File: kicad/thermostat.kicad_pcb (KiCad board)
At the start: 2 copper layers, 65 x 56 mm, 5 parts, among them P1 Conn_02x20_Odd_Even

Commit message: some board changes, probably too small...
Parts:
- added SW_DOWN1: SW_DOWN, Buttons_Switches_SMD:SW_SPST_EVPBF, F.Cu at (249.5, 141.7)
- added SW_ENTER1: SW_ENTER, Buttons_Switches_SMD:SW_SPST_EVPBF, F.Cu at (227.3, 141.7)
- added SW_MODE1: SW_MODE, Buttons_Switches_SMD:SW_SPST_EVPBF, F.Cu at (238.7, 141.7)
- added SW_UP1: SW_UP, Buttons_Switches_SMD:SW_SPST_EVPBF, F.Cu at (215.9, 141.7)
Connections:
- net +3V3 renamed /PWR_3.3V
- net +5V renamed /PWR_5V
- net GND renamed /GND
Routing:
- net /GPIO16: track 0.00 -> 54.5 mm
- net /GPIO21(SPI1_SCK): track 0.00 -> 52.2 mm
- net /GPIO17(GEN0): track 0.00 -> 49.2 mm
- net /GPIO22(GEN3): track 0.00 -> 46.6 mm
- added copper zone on B.Cu, net /GND
- added copper zone on F.Cu, net /PWR_3.3V
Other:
- outline, holes or cut-outs redrawn
- board text removed: "CAMERA"
- board text removed: "RASPBERRY-PI 40-PIN ADDON BOARD VIEW FROM TOP NOTE: P1 SHOULD BE FITTED ON THE REVERSE OF THE BOARD ADD EDGE CUTS FROM CAMERA AND DISPLAY PORTS AS REQUIRED"
- board text removed: "RJ45"
- board text removed: "USB"

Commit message: updates
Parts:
- added U1: PanasonicRelay, project_footprints:AGQ210A03, F.Cu at (281.3, 103.0)
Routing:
- net /GND: track 0.00 -> 32.8 mm
- net /PWR_5V: track 0.00 -> 2.54 mm
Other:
- net class Default: clearance 0.2 -> 0.127; trace_width 0.2 -> 0.127; via_dia 0.9 -> 0.4572; via_drill 0.6 -> 0.254
- net class Power: clearance 0.2 -> 0.127; trace_width 0.5 -> 0.127; via_dia 1 -> 0.4572; via_drill 0.7 -> 0.254
- rule trace_clearance: 0.2 -> 0.127
- rule trace_min: 0.1524 -> 0.127
- rule via_min_drill: 0.5 -> 0.254
- rule via_min_size: 0.8 -> 0.4572

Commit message: updates
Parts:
- added THERM_CONN1: THERM_CONN, TerminalBlocks_Phoenix:TerminalBlock_Phoenix_MPT-2.54mm_4pol, F.Cu at (257.1, 118.9)
- MK1, MK2, MK3, MK4: value M2.5 -> Mounting_Hole-Mechanical; footprint MountingHole:MountingHole_2.7mm_M2.5 -> Mounting_Holes:MountingHole_2.5mm_Pad
- U1: value PanasonicRelay -> RELAY_HEAT
- moved U1 61.5 mm to (221.0, 115.1)
- moved MK4 49.2 mm to (261.6, 97.3), turned to 180 degrees
- moved MK2 48.1 mm to (261.6, 145.6), turned to 0 degrees
- moved MK3 0.44 mm to (203.8, 146.2)
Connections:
- P1 pad 10: /GPIO15(RXD0) -> (no net)
- P1 pad 11: /GPIO17(GEN0) -> (no net)
- P1 pad 12: /GPIO18(GEN1)(PWM0) -> (no net)
- P1 pad 13: /GPIO27(GEN2) -> (no net)
- P1 pad 15: /GPIO22(GEN3) -> (no net)
- P1 pad 16: /GPIO23(GEN4) -> (no net)
- P1 pad 18: /GPIO24(GEN5) -> (no net)
- P1 pad 19: /GPIO10(SPI0_MOSI) -> (no net)
- P1 pad 21: /GPIO9(SPI0_MISO) -> (no net)
- P1 pad 22: /GPIO25(GEN6) -> (no net)
- P1 pad 23: /GPIO11(SPI0_SCK) -> (no net)
- P1 pad 24: /GPIO8(SPI0_CE_N) -> (no net)
- P1 pad 26: /GPIO7(SPI1_CE_N) -> (no net)
- P1 pad 27: /ID_SD -> (no net)
- P1 pad 28: /ID_SC -> (no net)
- P1 pad 3: /GPIO2(SDA1) -> (no net)
- P1 pad 33: /GPIO13(PWM1) -> (no net)
- P1 pad 35: /GPIO19(SPI1_MISO) -> (no net)
- P1 pad 37: /GPIO26 -> (no net)
- P1 pad 5: /GPIO3(SCL1) -> (no net)
- P1 pad 7: /GPIO4(GCLK) -> (no net)
- P1 pad 8: /GPIO14(TXD0) -> (no net)
- SW_ENTER1 pad 1: /GPIO22(GEN3) -> /GPIO12(PWM0)
- SW_UP1 pad 1: /GPIO17(GEN0) -> /GPIO20(SPI1_MOSI)
- U1 pad 1: Net-(U1-Pad1) -> /GPIO6
- U1 pad 2: Net-(U1-Pad2) -> (no net)
- U1 pad 3: Net-(U1-Pad3) -> (no net)
- U1 pad 4: Net-(U1-Pad4) -> (no net)
- U1 pad 5: Net-(U1-Pad5) -> (no net)
- U1 pad 6: Net-(U1-Pad6) -> /HVAC_PWR(RED)
- U1 pad 7: Net-(U1-Pad7) -> /HVAC_HEAT(WHITE)
- U1 pad 8: Net-(U1-Pad8) -> /GPIO5
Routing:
- net /GPIO17(GEN0): track 49.2 -> 0.00 mm
- net /GPIO16: track 54.5 -> 7.34 mm
- net /GPIO22(GEN3): track 46.6 -> 0.00 mm
- net /GPIO21(SPI1_SCK): track 52.2 -> 7.34 mm
- net /GPIO20(SPI1_MOSI): track 0.00 -> 5.76 mm
- net /GPIO12(PWM0): track 0.00 -> 5.76 mm

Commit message: First take at the bigger board
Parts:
- added G***: LOGO, project_footprints:LlamaHead, F.Cu at (138.5, 122.5)
- added RELAY_COOL1: RELAY_COOL, project_footprints:AGQ210A03, F.Cu at (218.2, 161.8)
- added RELAY_HEAT1: RELAY_HEAT, project_footprints:AGQ210A03, F.Cu at (218.2, 145.0)
- P1: moved to F.Cu
- RELAY_FAN1: renamed from U1; value RELAY_HEAT -> RELAY_FAN
- moved MK1 101.5 mm to (265.2, 178.0)
- moved SW_UP1 80.2 mm to (148.2, 184.9)
- moved THERM_CONN1 73.8 mm to (262.8, 192.5)
- moved SW_ENTER1 72.6 mm to (168.9, 184.9)
- moved SW_MODE1 65.3 mm to (189.6, 184.9)
- moved SW_DOWN1 58.3 mm to (210.3, 184.9)
- moved MK3 49.9 mm to (242.2, 178.0)
- moved P1 43.7 mm to (243.5, 124.8), turned to 0 degrees
- moved MK2 32.1 mm to (242.2, 120.0)
- moved MK4 23.0 mm to (265.2, 120.0)
- moved RELAY_FAN1 13.4 mm to (218.2, 128.2), turned to 270 degrees
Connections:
- P1 pad 33: (no net) -> /GPIO13(PWM1)
- P1 pad 35: (no net) -> /GPIO19(SPI1_MISO)
- RELAY_FAN1 pad 1: /GPIO6 -> /GPIO19(SPI1_MISO)
- RELAY_FAN1 pad 7: /HVAC_HEAT(WHITE) -> /HVAC_FAN(GREEN)
- THERM_CONN1 pad 3: (no net) -> /HVAC_COOL(YELLOW)
- THERM_CONN1 pad 4: (no net) -> /HVAC_FAN(GREEN)
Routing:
- net /GND: track 32.8 -> 0.00 mm
- net /GPIO21(SPI1_SCK): track 7.34 -> 0.00 mm
- net /GPIO16: track 7.34 -> 0.00 mm
- net /GPIO20(SPI1_MOSI): track 5.76 -> 0.00 mm
- net /GPIO12(PWM0): track 5.76 -> 0.00 mm
- net /PWR_5V: track 2.54 -> 0.00 mm
- removed copper zone on B.Cu, net /GND
- removed copper zone on F.Cu, net /PWR_3.3V
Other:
- board size 65 x 56 mm -> 138 x 80 mm
- board text added: "RaspberryPi Zero"
- board text removed: "DISPLAY"

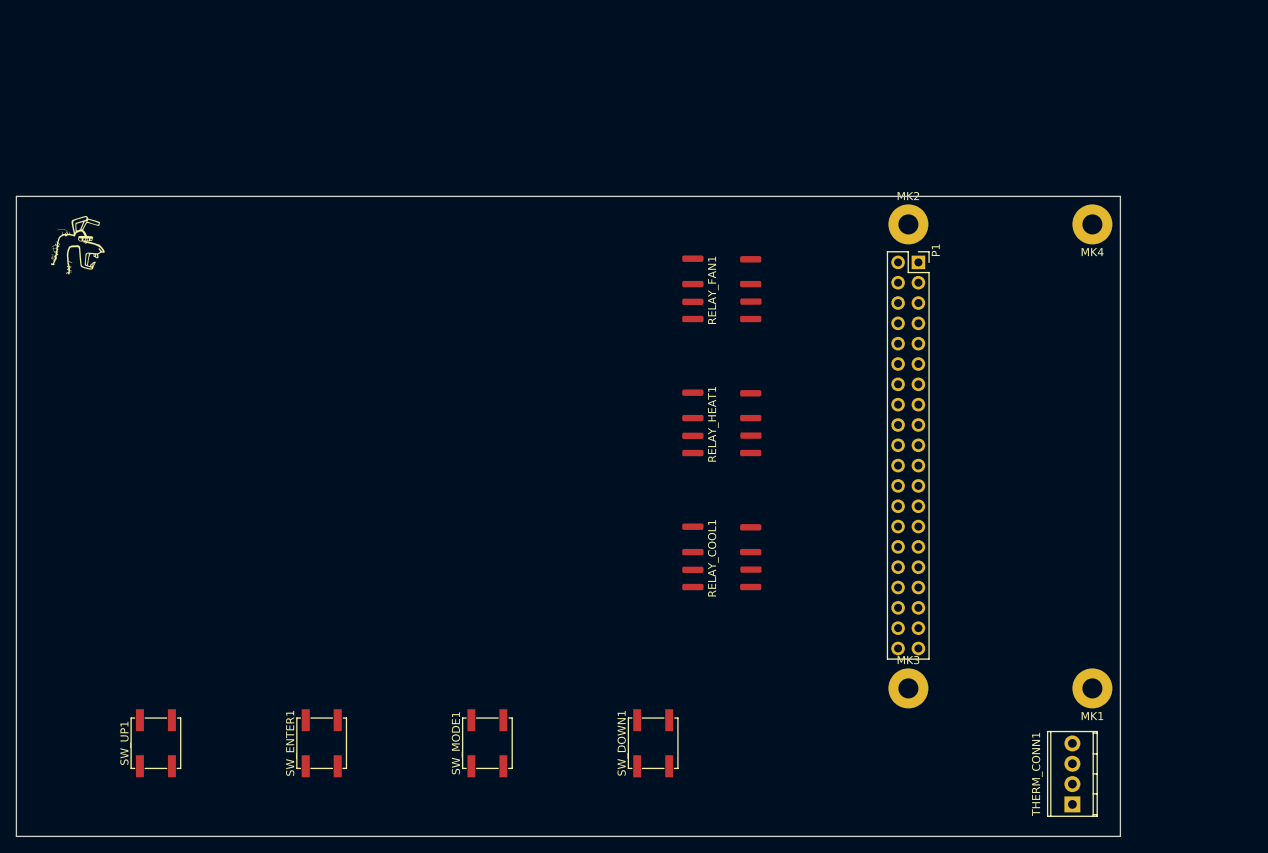
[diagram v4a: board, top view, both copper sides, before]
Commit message: Almost ready for ethernet header
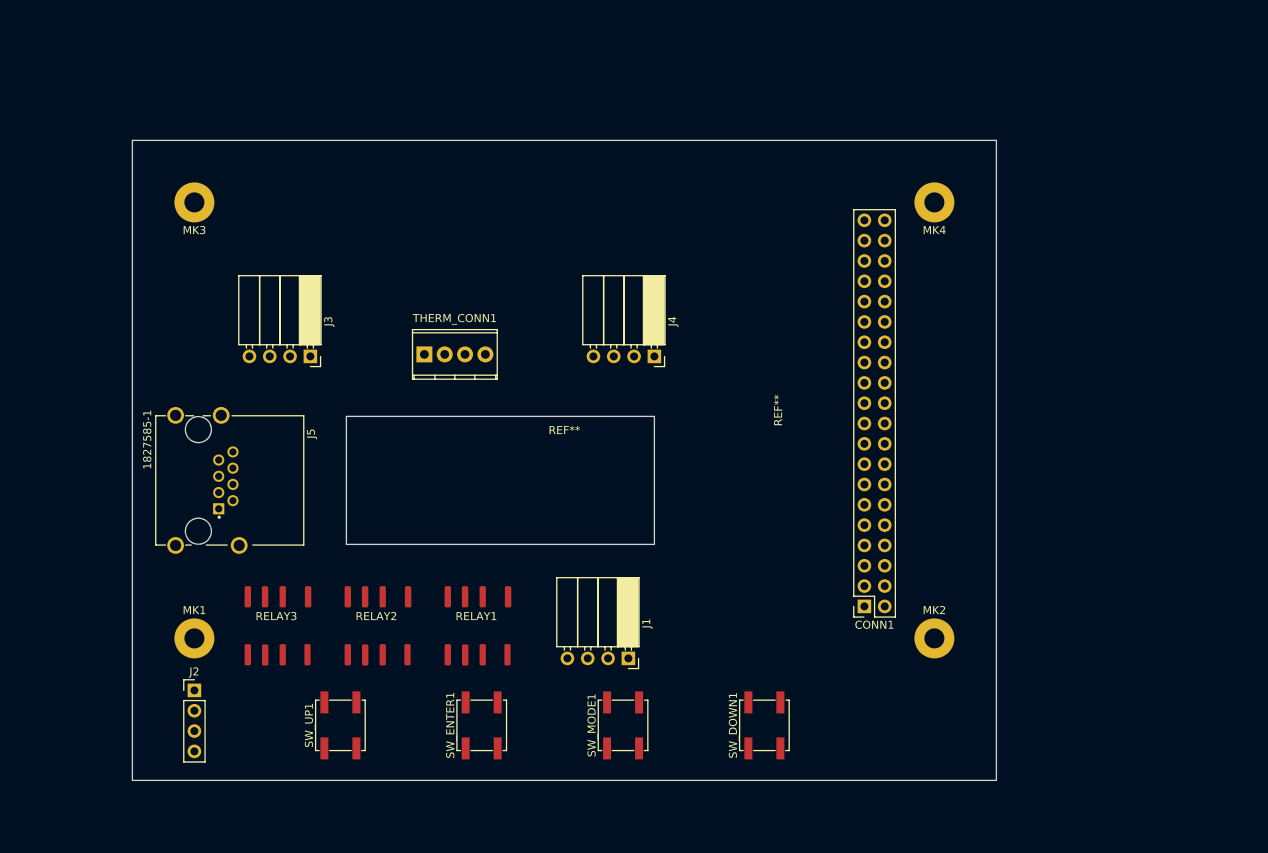
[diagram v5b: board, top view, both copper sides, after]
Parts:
- removed G***: LOGO, project_footprints:LlamaHead
- added J1: Display i2c, Socket_Strips:Socket_Strip_Angled_1x04_Pitch2.54mm, F.Cu at (207.2, 174.2)
- added J2: Sensor i2c, Socket_Strips:Socket_Strip_Straight_1x04_Pitch2.54mm, F.Cu at (153.0, 178.2)
- added J3: PoE Input, Socket_Strips:Socket_Strip_Angled_1x04_Pitch2.54mm, F.Cu at (167.5, 136.5)
- added J4: PoE Output, Socket_Strips:Socket_Strip_Angled_1x04_Pitch2.54mm, F.Cu at (210.5, 136.5)
- added J5: 1827585-1, project_footprints:TE_1827585-1, F.Cu at (153.5, 152.0)
- added REF**: RasperryPi_Zero, project_footprints:RasperryPi_Zero, F.Cu at (226.5, 143.2)
- added REF**: 20X4_LCD, project_footprints:20X4_LCD, F.Cu at (199.2, 144.5)
- CONN1: renamed from P1; footprint Connector_PinSocket_2.54mm:PinSocket_2x20_P2.54mm_Vertical -> Socket_Strips:Socket_Strip_Straight_2x20_Pitch2.54mm
- moved MK1 112.4 mm to (153.0, 171.8), turned to 0 degrees
- moved MK3 108.0 mm to (153.0, 117.2), turned to 180 degrees
- moved THERM_CONN1 98.6 mm to (181.8, 136.2), turned to 0 degrees
- moved RELAY3 55.5 mm to (163.2, 169.5), turned to 180 degrees
- moved MK2 51.9 mm to (245.5, 171.8)
- moved RELAY1 51.0 mm to (188.2, 169.5), turned to 180 degrees
- moved RELAY2 49.1 mm to (175.8, 169.5), turned to 180 degrees
- moved CONN1 43.5 mm to (236.8, 167.8), turned to 180 degrees
- moved SW_UP1 23.2 mm to (171.2, 182.6)
- moved SW_ENTER1 20.1 mm to (188.9, 182.6)
- moved MK4 19.9 mm to (245.5, 117.2)
- moved SW_MODE1 17.1 mm to (206.6, 182.6)
- moved SW_DOWN1 14.1 mm to (224.2, 182.6)
- renumbered RELAY_FAN1 to RELAY1, RELAY_HEAT1 to RELAY2, RELAY_COOL1 to RELAY3
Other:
- board size 138 x 80 mm -> 108 x 80 mm
- board text removed: "RaspberryPi Zero"

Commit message: Ready for checkout and routing
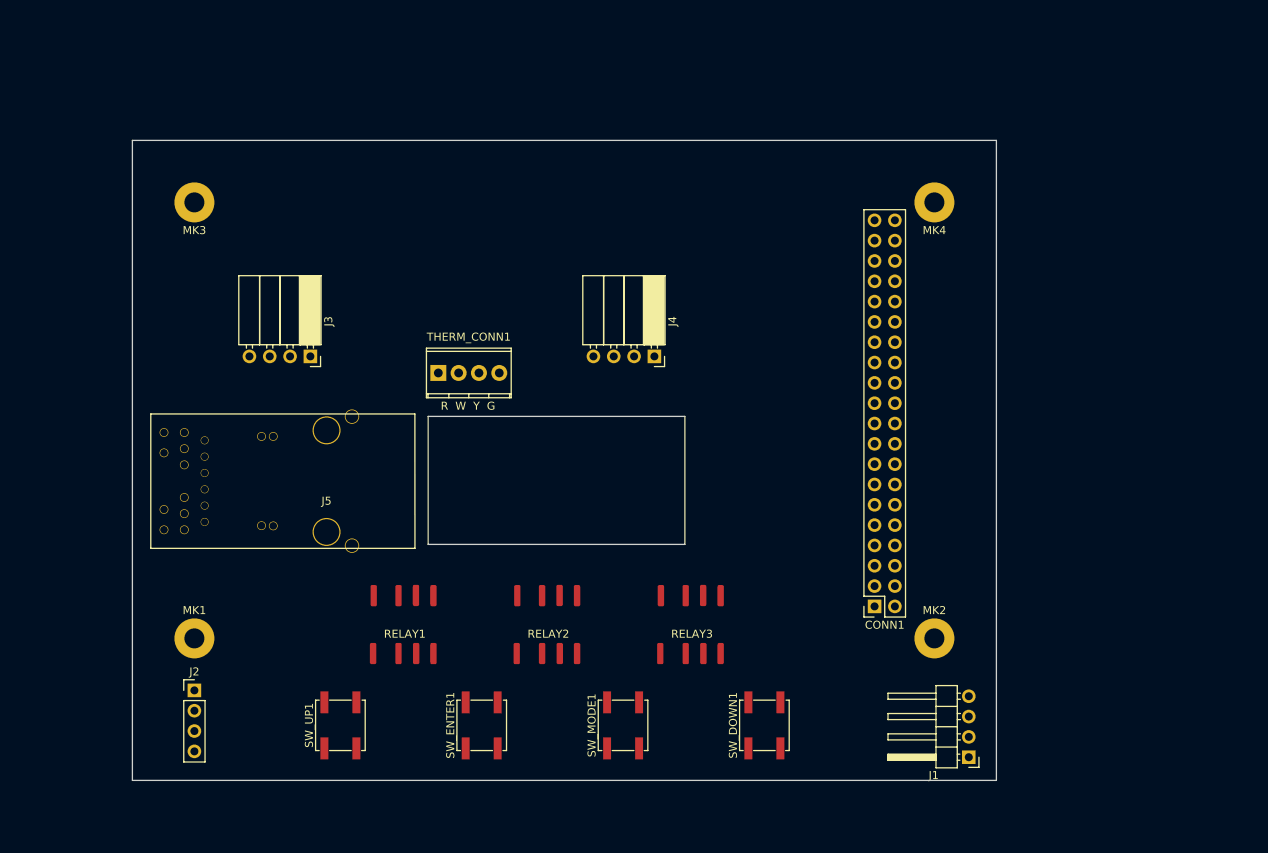
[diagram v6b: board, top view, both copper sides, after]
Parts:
- removed REF**: RasperryPi_Zero, project_footprints:RasperryPi_Zero
- removed REF**: 20X4_LCD, project_footprints:20X4_LCD
- J1: footprint Socket_Strips:Socket_Strip_Angled_1x04_Pitch2.54mm -> Pin_Headers:Pin_Header_Angled_1x04_Pitch2.54mm
- J5: value 1827585-1 -> 0857891001; footprint project_footprints:TE_1827585-1 -> project_footprints:0857891001
- moved RELAY3 52.0 mm to (215.2, 170.7), turned to 0 degrees
- moved J1 44.3 mm to (249.8, 186.6), turned to 180 degrees
- moved RELAY2 21.5 mm to (197.2, 170.7), turned to 0 degrees
- moved J5 16.0 mm to (169.5, 152.1), turned to 0 degrees
- moved RELAY1 9.03 mm to (179.3, 170.7), turned to 0 degrees
- moved THERM_CONN1 2.90 mm to (183.5, 138.6)
- moved CONN1 1.27 mm to (238.0, 167.8)
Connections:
- CONN1 pad 3: (no net) -> /GPIO2(SDA1)
- CONN1 pad 5: (no net) -> /GPIO3(SCL1)
- J1 pad 1: (no net) -> /GND
- J1 pad 2: (no net) -> /PWR_5V
- J1 pad 3: (no net) -> /GPIO2(SDA1)
- J1 pad 4: (no net) -> /GPIO3(SCL1)
- J2 pad 1: (no net) -> /GPIO2(SDA1)
- J2 pad 2: (no net) -> /GPIO3(SCL1)
- J2 pad 3: (no net) -> /GND
- J2 pad 4: (no net) -> /PWR_5V
- J3 pad 1: (no net) -> Net-(J3-Pad1)
- J4 pad 1: (no net) -> /GND
- J4 pad 2: (no net) -> /PWR_5V
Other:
- outline, holes or cut-outs redrawn
- board text added: "R W Y G"

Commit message: Re-arrange board; still need measurements
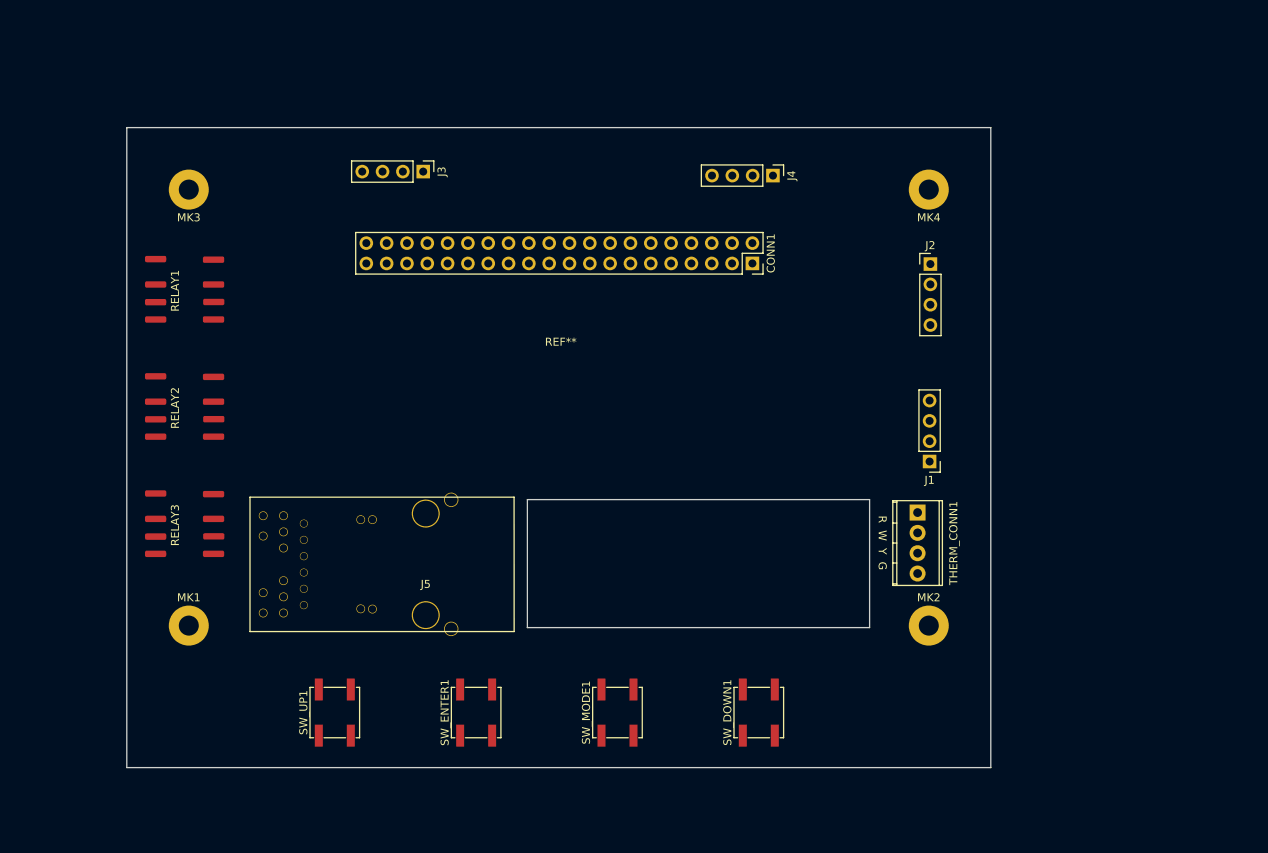
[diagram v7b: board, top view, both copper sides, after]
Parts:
- added REF**: RasperryPi_Zero, project_footprints:RasperryPi_Zero, F.Cu at (198.8, 135.2)
- J1: footprint Pin_Headers:Pin_Header_Angled_1x04_Pitch2.54mm -> Pin_Headers:Pin_Header_Straight_1x04_Pitch2.54mm
- J3, J4: footprint Socket_Strips:Socket_Strip_Angled_1x04_Pitch2.54mm -> Pin_Headers:Pin_Header_Straight_1x04_Pitch2.54mm
- moved J2 106.3 mm to (245.0, 125.0)
- moved RELAY3 65.4 mm to (151.1, 157.6), turned to 270 degrees
- moved THERM_CONN1 62.4 mm to (243.4, 156.0), turned to 270 degrees
- moved RELAY2 53.9 mm to (151.1, 142.9), turned to 270 degrees
- moved RELAY1 50.9 mm to (151.1, 128.3), turned to 270 degrees
- moved CONN1 45.5 mm to (222.8, 124.9), turned to 270 degrees
- moved J1 37.3 mm to (244.9, 149.6)
- moved J3 27.1 mm to (181.6, 113.4)
- moved J4 27.0 mm to (225.3, 113.9)
- moved J5 16.2 mm to (181.9, 162.5)
- moved SW_MODE1 1.75 mm to (205.9, 181.0)
- moved MK1 1.75 mm to (152.3, 170.2)
- moved MK2 1.75 mm to (244.8, 170.2)
- moved MK3 1.75 mm to (152.3, 115.7)
- moved MK4 1.75 mm to (244.8, 115.7)
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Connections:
- SW_DOWN1 pad 2: /PWR_3.3V -> /PWR_5V
- SW_ENTER1 pad 2: /PWR_3.3V -> /PWR_5V
- SW_MODE1 pad 2: /PWR_3.3V -> /PWR_5V
- SW_UP1 pad 2: /PWR_3.3V -> /PWR_5V
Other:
- outline, holes or cut-outs redrawn

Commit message: more updates, backstop before 24v conversation
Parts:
- J3, J4: footprint Pin_Headers:Pin_Header_Straight_1x04_Pitch2.54mm -> project_footprints:M20-7910542R
- moved CONN1 53.2 mm to (176.0, 150.3), turned to 90 degrees
- moved J4 45.5 mm to (179.9, 116.6), turned to 0 degrees
- moved J3 39.1 mm to (220.6, 116.6), turned to 0 degrees
- moved REF** 5.00 mm to (199.8, 140.1)
- moved SW_MODE1 3.42 mm to (208.6, 183.1)
- moved SW_DOWN1 3.42 mm to (226.2, 183.1)
- moved SW_ENTER1 3.42 mm to (190.9, 183.1)
- moved SW_UP1 3.42 mm to (173.2, 183.1)
- moved J2 2.82 mm to (246.3, 127.5)
- moved J5 2.82 mm to (183.2, 165.0)
- moved RELAY1 2.82 mm to (152.4, 130.8)
- moved RELAY2 2.82 mm to (152.4, 145.4)
- moved RELAY3 2.82 mm to (152.4, 160.1)
- moved J1 2.82 mm to (246.2, 152.1)
- moved MK1 2.82 mm to (153.6, 172.7)
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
